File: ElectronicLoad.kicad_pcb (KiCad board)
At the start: 4 copper layers, 100 x 65 mm, 97 parts, among them J1 USB_B, J2 Load, J3 AUX1, J4 TagConnect, J5 ICSP, Q1 MTP3055VL, Q2 DMG2302U, SW2 RESET, SW3 BOOTLOADER, SW4 Control, U1 TLC272, U2 NUP2114, U3 ATmega32U4-AU, U4 MCP1501-20, U5 MCP4726A3T, U6 INA220, U7 PCT2075D, U8 PCT2075D, Y1 16MHz

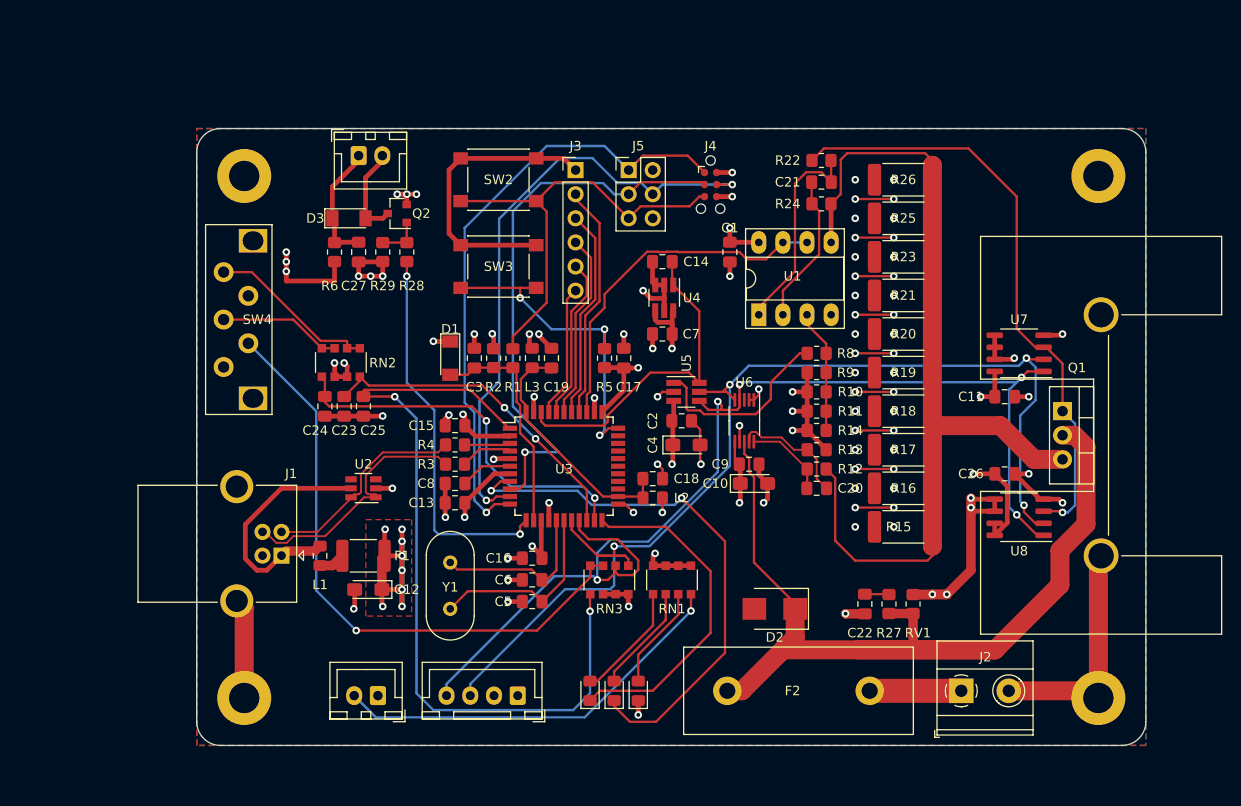
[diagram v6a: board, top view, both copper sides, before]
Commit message: Move input connector, routing, silkscreen
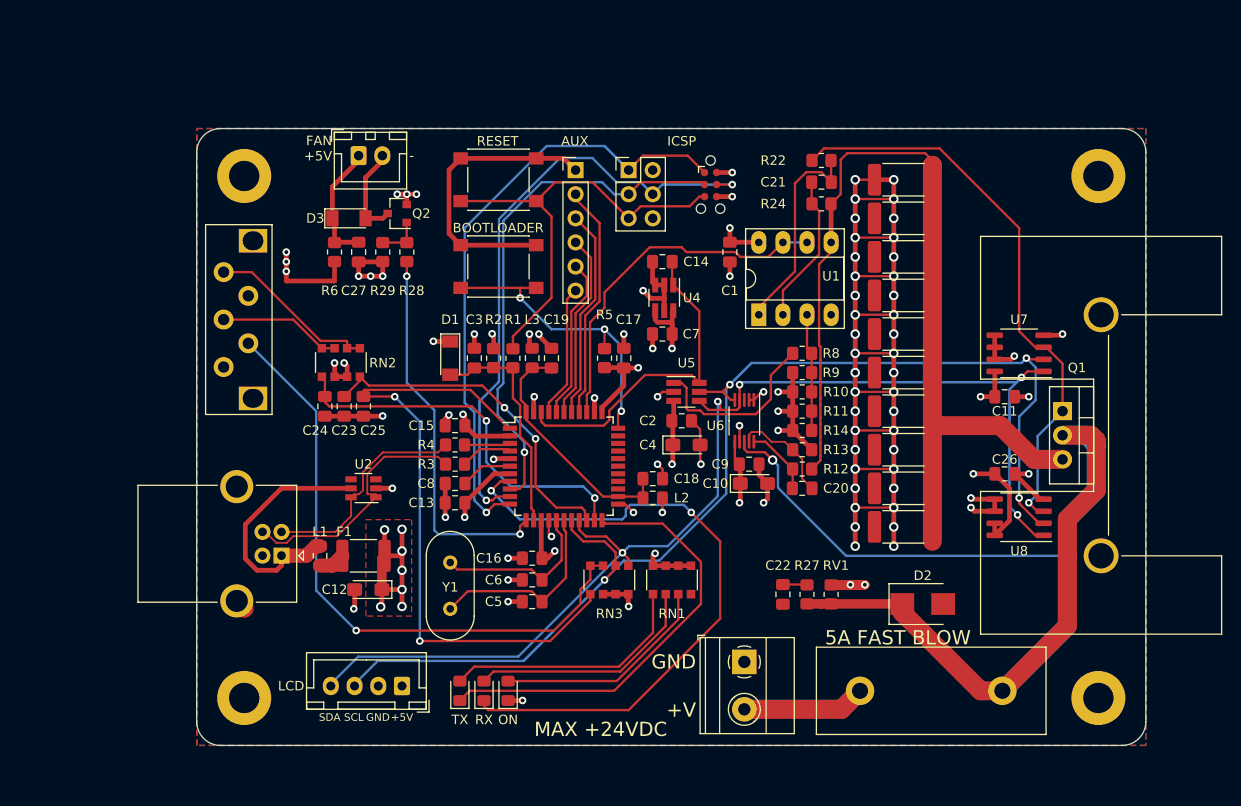
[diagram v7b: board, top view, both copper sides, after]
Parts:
- removed LED4: POWER-CASE, Connector_JST:JST_XH_B2B-XH-A_1x02_P2.50mm_Vertical
- moved J2 23.1 mm to (107.7, 171.2), turned to 270 degrees
- moved D2 15.6 mm to (126.5, 165.1), turned to 0 degrees
- moved LED2 13.7 mm to (80.3, 174.2)
- moved LED1 13.7 mm to (77.7, 174.2)
- moved LED3 13.7 mm to (82.8, 174.2)
- moved LCD1 12.2 mm to (71.6, 173.7)
- moved R27 8.70 mm to (114.3, 164.1)
- moved C22 8.70 mm to (111.8, 164.1)
- moved RV1 8.70 mm to (116.8, 164.1)
- moved C20 1.52 mm to (113.8, 152.9)
- moved R10 1.52 mm to (113.8, 142.7)
- moved R11 1.52 mm to (113.8, 144.8)
- moved R12 1.52 mm to (113.8, 150.9)
- moved R13 1.52 mm to (113.8, 148.8)
- moved R14 1.52 mm to (113.8, 146.8)
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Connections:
- J2 pad 1: /LOAD -> GND
- J2 pad 2: GND -> /LOAD
- RN3 pad 1: SCL -> SDA
- RN3 pad 2: SDA -> SCL
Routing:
- net GND: track 249.1 -> 301.2 mm
- net Net-(RN1-Pad8): track 42.8 -> 0.00 mm, vias 1 -> 0
- net VLOAD: track 103.9 -> 134.4 mm, vias 0 -> 1
- net /LOAD: track 9.65 -> 26.0 mm
- net ROT_SW: track 83.5 -> 68.3 mm
- net Net-(LED1-Pad2): track 12.4 -> 26.5 mm
- net Net-(LED2-Pad2): track 11.4 -> 24.9 mm
- net Net-(LED3-Pad2): track 10.9 -> 23.3 mm
- net ~RXLED: track 57.5 -> 68.2 mm
- net ~TXLED: track 35.8 -> 46.3 mm
- net SCL: track 121.2 -> 128.6 mm
- net VCC: track 128.7 -> 122.0 mm, vias 30 -> 29
- net /ILOAD+: track 97.0 -> 101.1 mm
- net /SCK: track 58.6 -> 54.9 mm
- net SDA: track 123.9 -> 127.4 mm
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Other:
- net class LOAD: via_drill 0.4 -> 0.6
- net class POWER: via_dia 0.8 -> 1; via_drill 0.4 -> 0.6
- rule pad_to_mask_clearance: 0 -> 0.05
- board text added: "+5V"
- board text added: "+V"
- board text added: "-"
- board text added: "5A FAST BLOW"
- board text added: "A1"
- board text added: "A2"
- board text added: "A3"
- board text added: "A4"
- board text added: "A5"
- board text added: "AUX"
- board text added: "BOOTLOADER"
- board text added: "Electronic Load Rev A 2021 Dominic Thibodeau https://github.com/hotkeysoft/electronicLoad-kicad dev@hotkeysoft.net"
- board text added: "FAN +5V"
- board text added: "GND"
- board text added: "ICSP"
- board text added: "LCD"
- board text added: "MAX +24VDC"
- board text added: "MISO"
- board text added: "MOSI"
- board text added: "ON"
- board text added: "RESET"
- board text added: "RST"
- board text added: "RX"
- board text added: "SCK"
- board text added: "SCL"
- board text added: "SDA"
- board text added: "TX"
- board text added: "VCC"

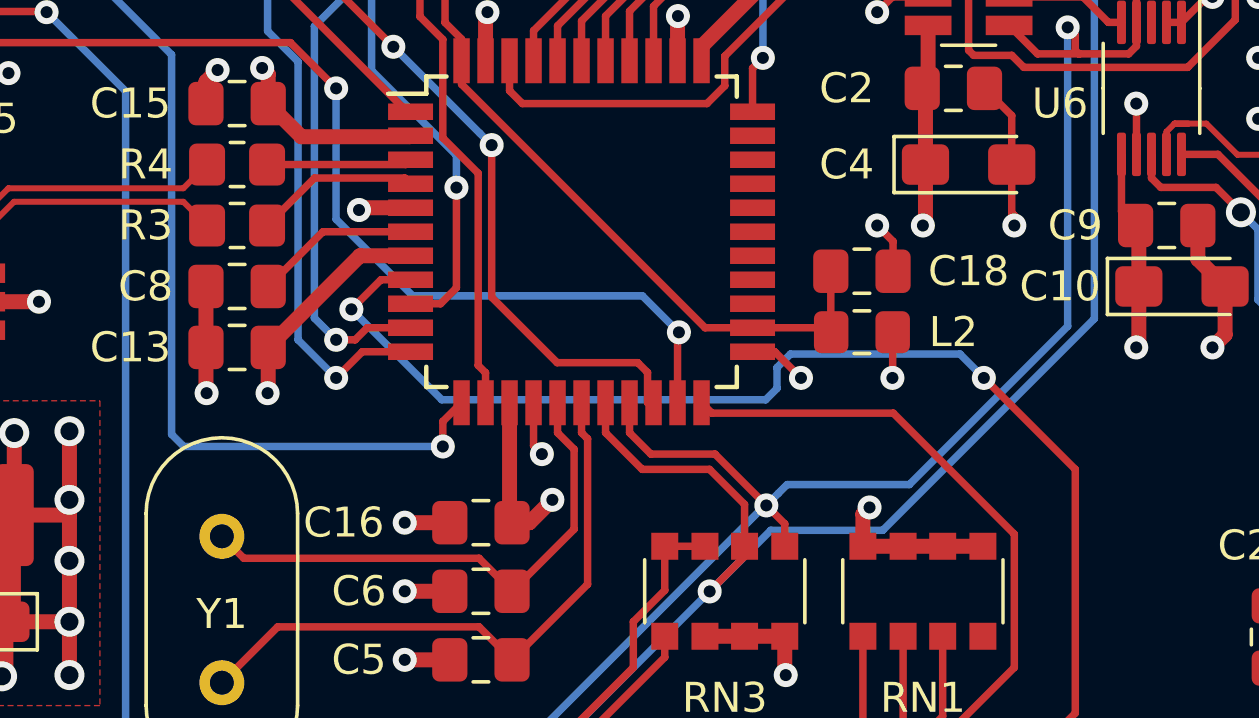
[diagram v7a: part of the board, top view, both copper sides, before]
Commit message: Move FAN_PWM to D10
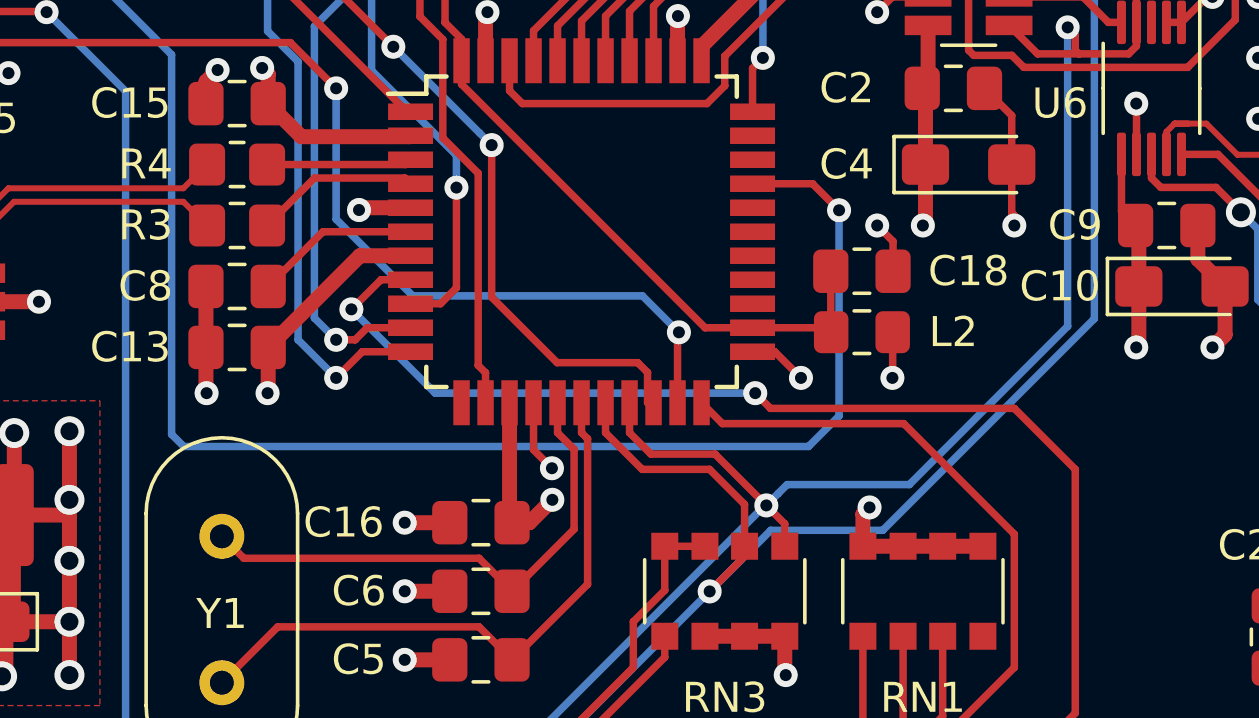
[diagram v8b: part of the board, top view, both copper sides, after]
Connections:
- U3 pad 12: FAN_PWM -> /D11
- U3 pad 30: /D10 -> FAN_PWM
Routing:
- net FAN_PWM: track 40.4 -> 62.5 mm
- net ~RXLED: track 68.2 -> 66.5 mm
- net GND: track 301.2 -> 301.8 mm
